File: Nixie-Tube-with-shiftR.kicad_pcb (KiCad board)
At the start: 2 copper layers, 35.5 x 44 mm, 55 parts, among them J1 Conn_01x05_Male, J2 Conn_01x01_Female, J3 Conn_01x05_Female, J4 Conn_01x01_Male, Q1 MMBTA42LT1, Q10 MMBTA42LT1, Q11 AO3400, Q12 AO3400, Q13 AO3400, Q14 MMBTA42LT1, Q15 MMBTA42LT1, Q2 MMBTA42LT1, Q3 MMBTA42LT1, Q4 MMBTA42LT1, Q5 MMBTA42LT1, Q6 MMBTA42LT1, Q7 MMBTA42LT1, Q8 MMBTA42LT1, Q9 MMBTA42LT1, U1 74HC595D, U2 nixie-tube, U3 74HC595D, U4 ams1117-5.0

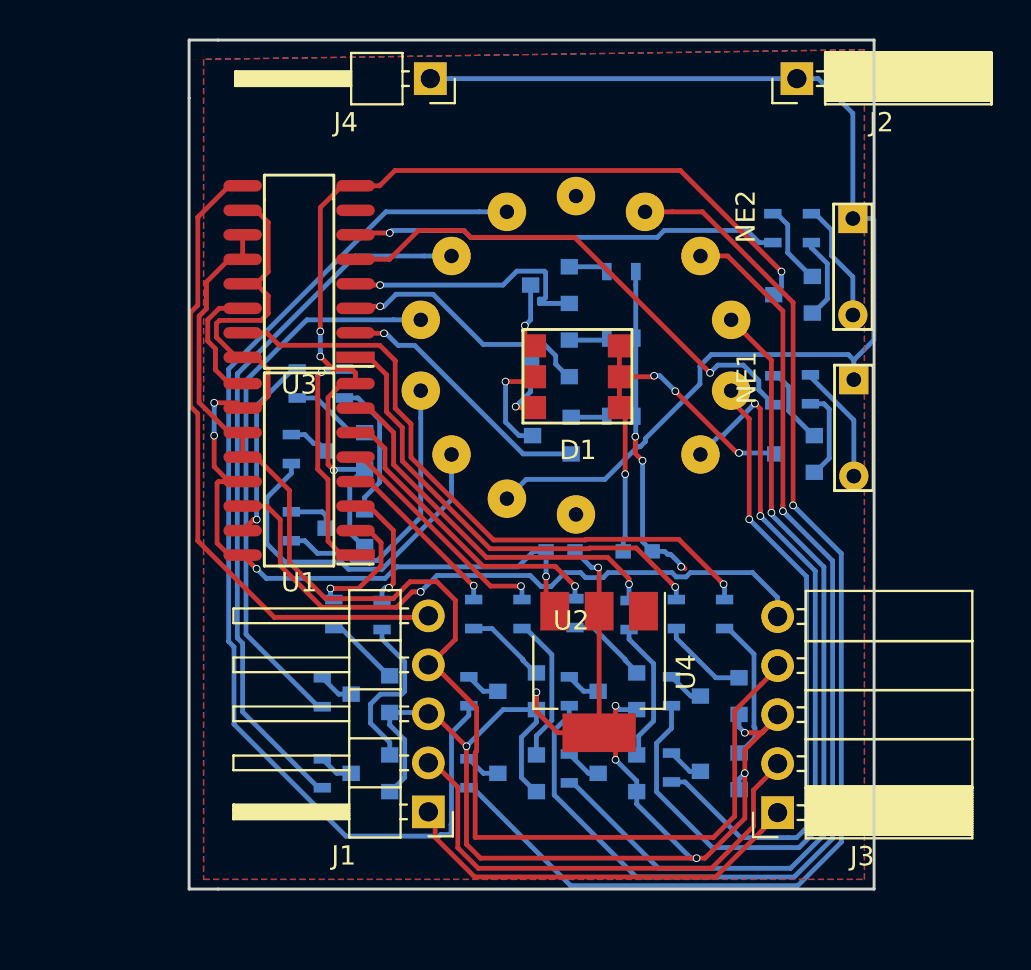
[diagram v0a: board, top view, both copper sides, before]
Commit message: modify board layout dimension text
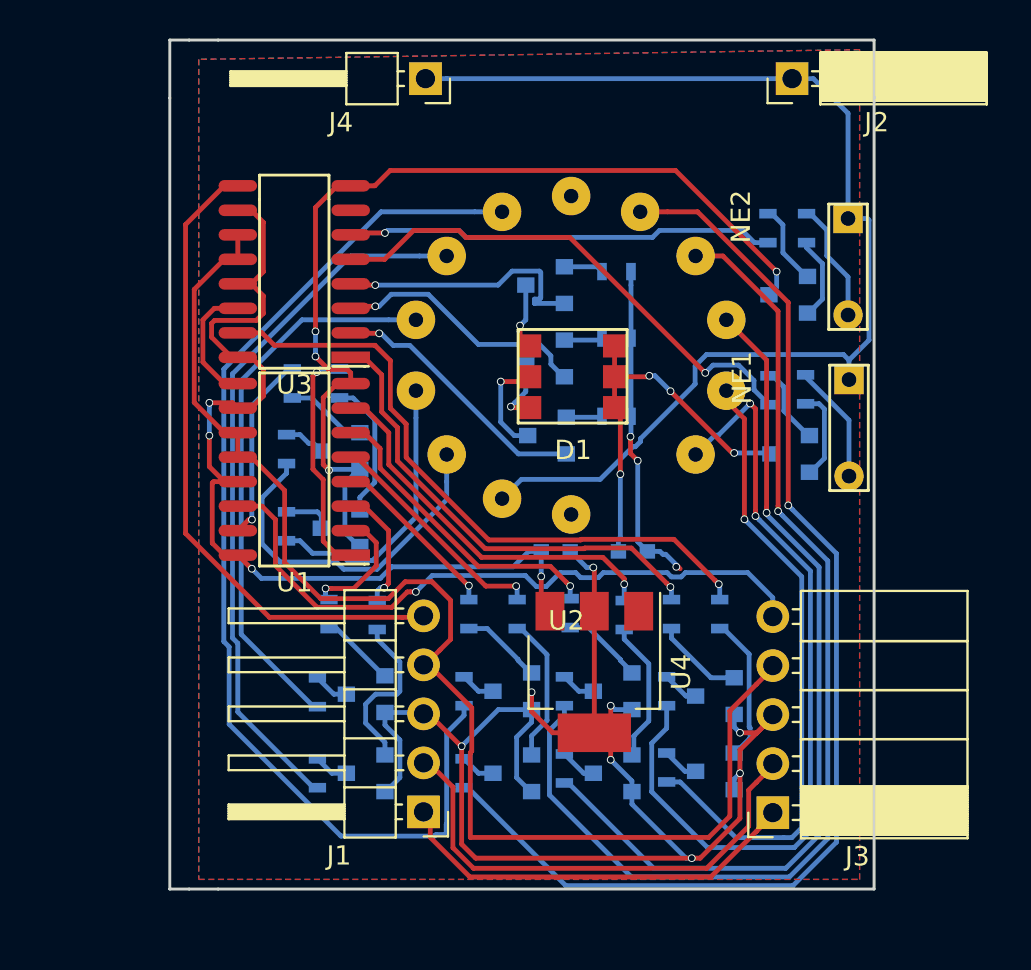
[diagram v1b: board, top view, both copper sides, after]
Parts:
- moved C1 0.25 mm to (175.5, 70.5)
- moved C2 0.25 mm to (171.5, 70.5)
- moved D1 0.25 mm to (172.4, 61.4)
- moved J1 0.25 mm to (164.7, 84.0)
- moved J2 0.25 mm to (183.8, 46.0)
- moved J3 0.25 mm to (182.8, 84.0)
- moved J4 0.25 mm to (164.8, 46.0)
- moved NE1 0.25 mm to (186.7, 61.6)
- moved NE2 0.25 mm to (186.7, 53.2)
- moved Q1 0.25 mm to (160.3, 65.3)
- moved Q10 0.25 mm to (169.2, 77.8)
- moved Q11 0.25 mm to (171.1, 64.5)
- moved Q12 0.25 mm to (170.9, 60.5)
- moved Q13 0.25 mm to (170.9, 56.7)
- moved Q14 0.25 mm to (183.7, 65.5)
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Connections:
- J1 pad 5: /MOSI -> /MOSI-OUT
- J3 pad 5: /MOSI-OUT -> /MOSI
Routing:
- net /MOSI: track 45.5 -> 34.6 mm
- net /MOSI-OUT: track 22.7 -> 33.7 mm
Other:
- board size 35.5 x 44 mm -> 36.5 x 44 mm
- board text added: "36.5x44mm"
- board text removed: "34x44mm"

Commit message: fix track being too near to border line
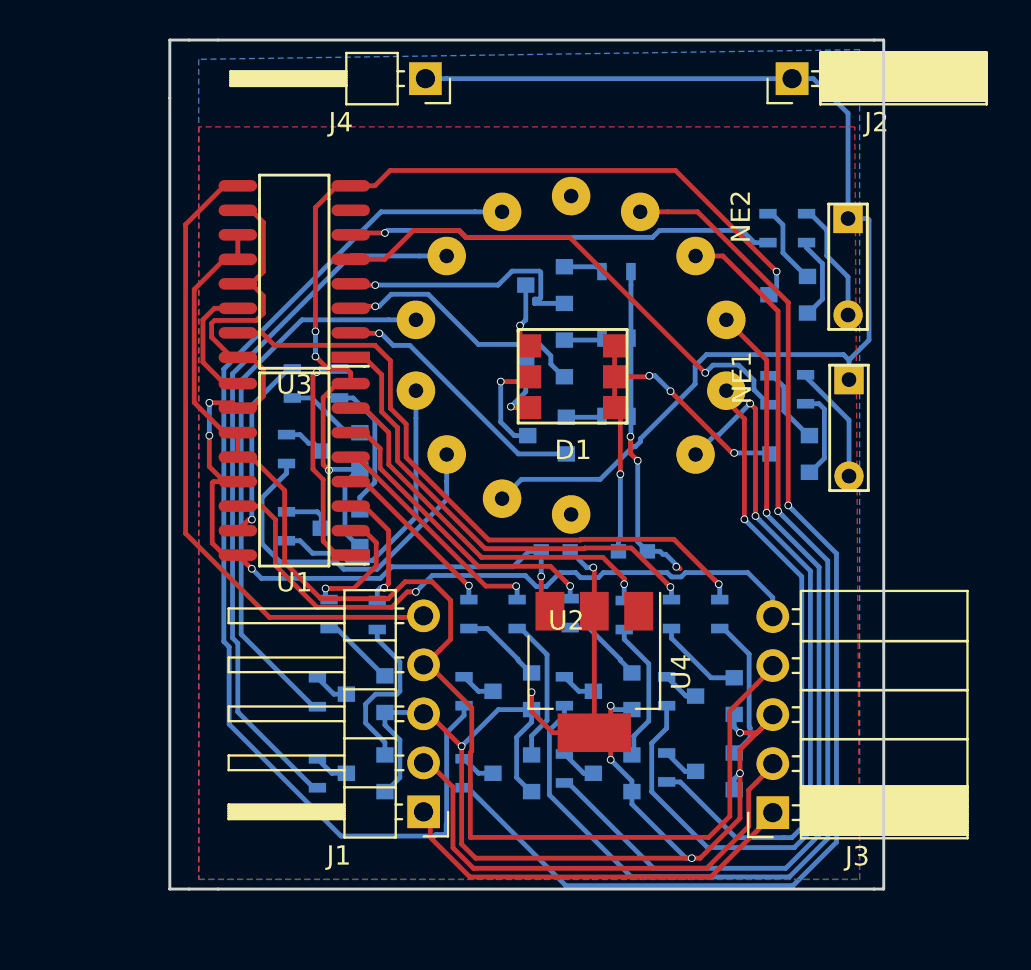
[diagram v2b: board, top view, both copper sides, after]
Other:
- board size 36.5 x 44 mm -> 37 x 44 mm
- board text added: "37x44mm"
- board text removed: "36.5x44mm"
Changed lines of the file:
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@@
     (links 105)
     (no_connects 0)
-    (area 151.424999 43.924999 188.075001 88.075001)
+    (area 151.424999 42.755 195.925239 91.35)
     (thickness 1.6)
-    (drawings 11)
+    (drawings 13)
     (tracks 662)
     (zones 0)
@@
     )
   )
+  (gr_line (start 188.5 88) (end 188 88) (layer Edge.Cuts) (width 0.15))
+  (gr_line (start 188 44) (end 188.5 44) (layer Edge.Cuts) (width 0.15))
   (gr_line (start 152.5 88) (end 151.5 88) (layer Edge.Cuts) (width 0.15))
   (gr_line (start 152.5 44) (end 151.5 44) (layer Edge.Cuts) (width 0.15))
   (gr_line (start 154 88) (end 152.5 88) (layer Edge.Cuts) (width 0.15))
   (gr_line (start 154 44) (end 152.5 44) (layer Edge.Cuts) (width 0.15))
-  (gr_text 36.5x44mm (at 170.25 90) (layer Eco1.User)
+  (gr_text 37x44mm (at 170.25 90) (layer Eco1.User)
     (effects (font (size 1.5 1.5) (thickness 0.3)))
   )
-  (gr_line (start 188 44) (end 188 47) (layer Edge.Cuts) (width 0.15))
+  (gr_line (start 188.5 44) (end 188.5 47) (layer Edge.Cuts) (width 0.15))
   (gr_line (start 154 44) (end 188 44) (layer Edge.Cuts) (width 0.15))
   (gr_line (start 151.5 47) (end 151.5 44) (layer Edge.Cuts) (width 0.15))
-  (gr_line (start 188 88) (end 188 47) (layer Edge.Cuts) (width 0.15))
+  (gr_line (start 188.5 88) (end 188.5 47) (layer Edge.Cuts) (width 0.15))
   (gr_line (start 154 88) (end 188 88) (layer Edge.Cuts) (width 0.15))
   (gr_line (start 151.5 47) (end 151.5 88) (layer Edge.Cuts) (width 0.15))
@@
     (polygon
       (pts
-        (xy 153 45) (xy 153 87.5) (xy 187.25 87.5) (xy 187.25 44.5)
+        (xy 153 48.5) (xy 153 87.5) (xy 187.25 87.5) (xy 187 48.5)
       )
     )

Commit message: modify 9V gnd tracks bigger
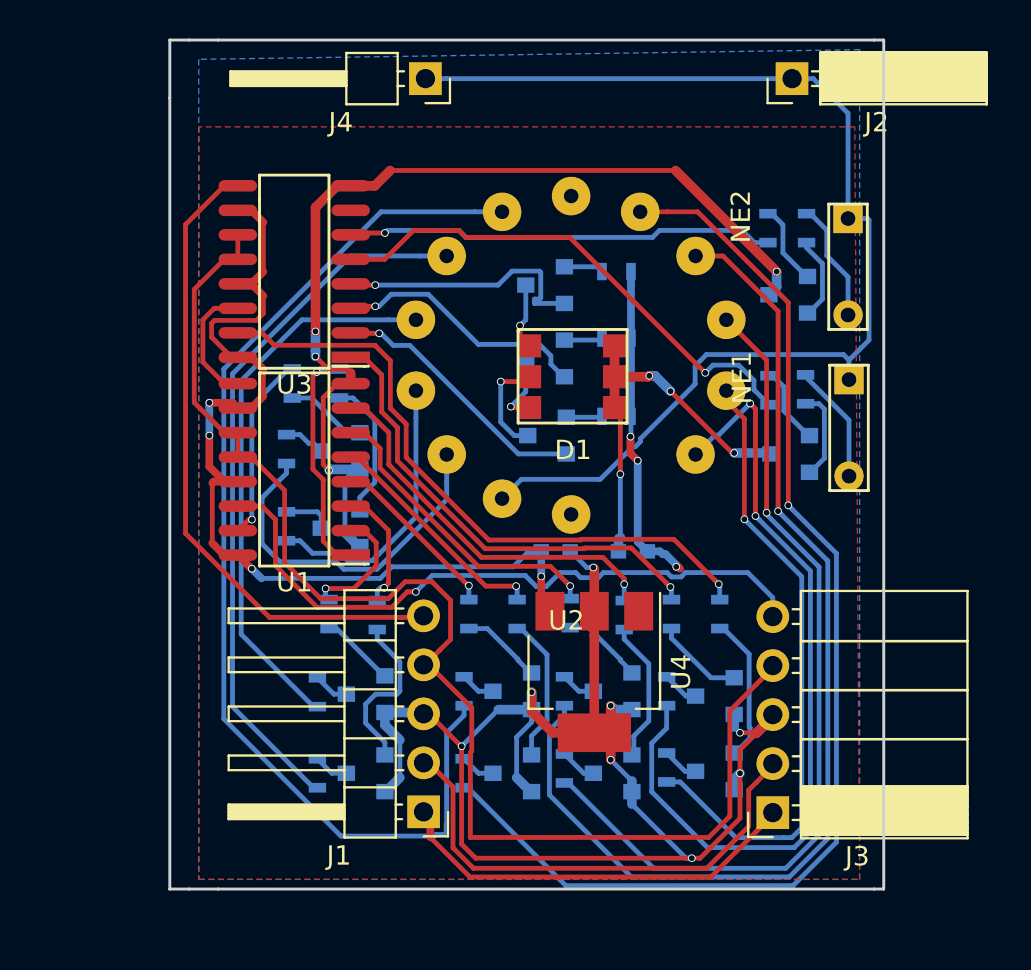
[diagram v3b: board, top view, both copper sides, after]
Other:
- net class GND added: clearance 0.2, trace_width 0.5, via_dia 0.4, via_drill 0.3

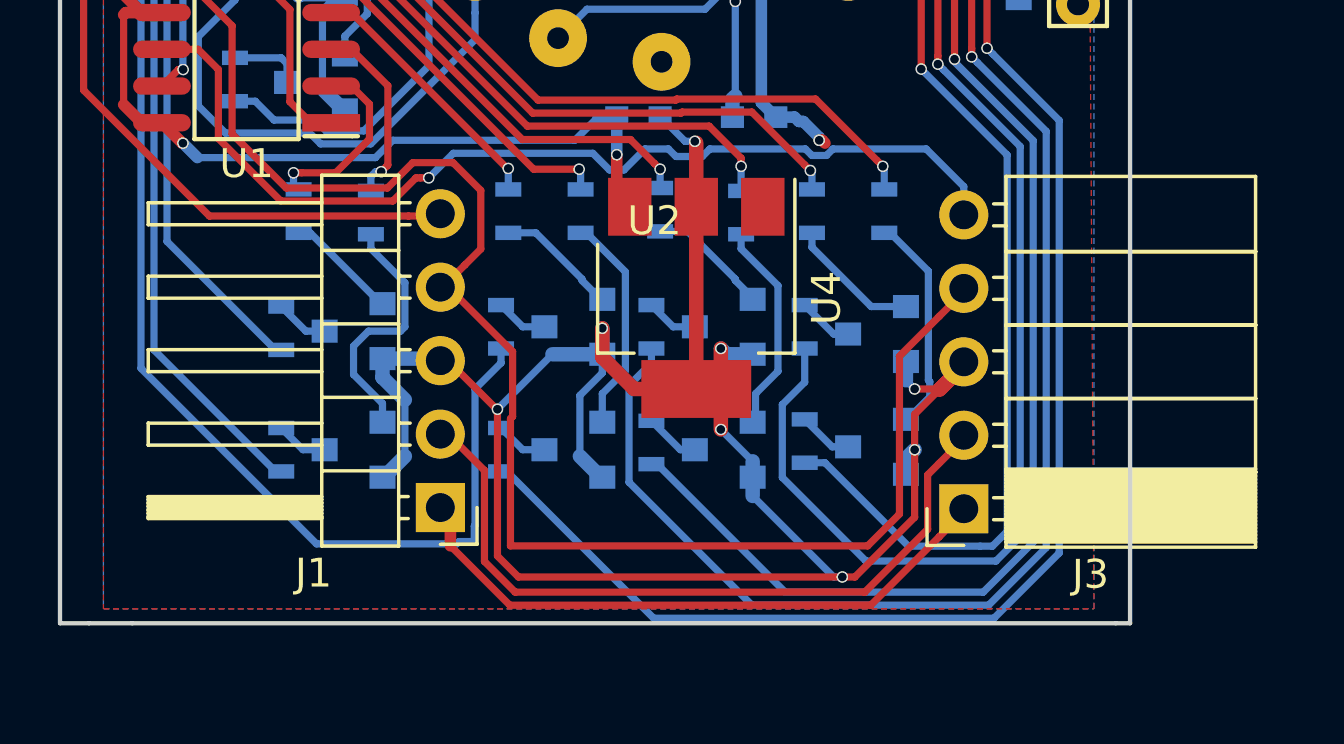
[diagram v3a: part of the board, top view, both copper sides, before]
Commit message: added OE to the pins
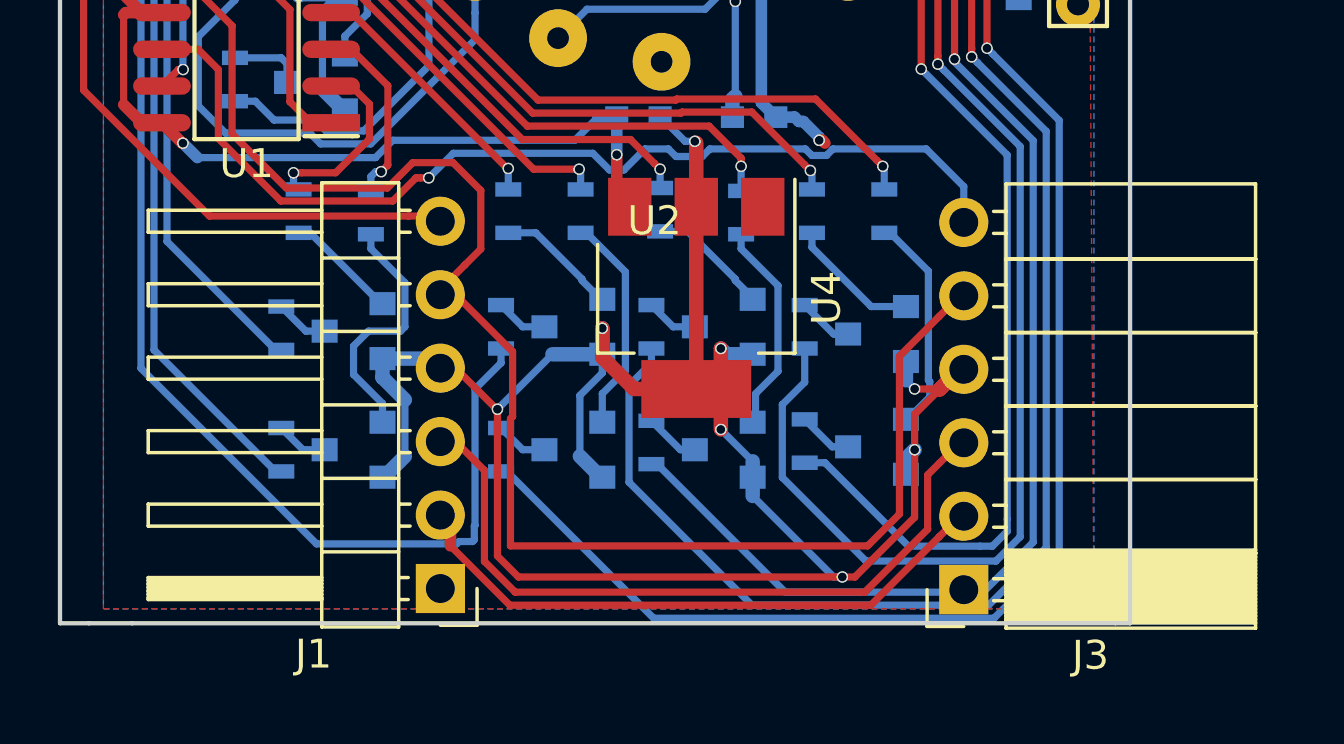
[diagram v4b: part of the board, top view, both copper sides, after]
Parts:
- J1: value Conn_01x05_Male -> Conn_01x06_Male; footprint Pin_Headers:Pin_Header_Angled_1x05_Pitch2.54mm -> Pin_Headers:Pin_Header_Angled_1x06_Pitch2.54mm
- J3: value Conn_01x05_Female -> Conn_01x06_Female; footprint Socket_Strips:Socket_Strip_Angled_1x05_Pitch2.54mm -> Socket_Strips:Socket_Strip_Angled_1x06_Pitch2.54mm
- moved J1 2.80 mm to (164.7, 86.8)
- moved J3 2.80 mm to (182.8, 86.8)
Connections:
- J1 pad 1: +9V -> Net-(J1-Pad1)
- J1 pad 2: /PWREN -> +9V
- J1 pad 3: GND -> /PWREN
- J1 pad 4: /SCK -> GND
- J1 pad 5: /MOSI-OUT -> /SCK
- J3 pad 1: +9V -> Net-(J1-Pad1)
- J3 pad 2: /PWREN -> +9V
- J3 pad 3: GND -> /PWREN
- J3 pad 4: /SCK -> GND
- J3 pad 5: /MOSI -> /SCK
- U1 pad 13: +5V -> Net-(J1-Pad1)
- U3 pad 13: +5V -> Net-(J1-Pad1)
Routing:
- net Net-(J1-Pad1): track 0.00 -> 26.8 mm
- net GND: track 147.8 -> 172.7 mm, vias 16 -> 15
- net /MOSI: track 34.6 -> 12.8 mm, vias 1 -> 0
- net /SCK: track 67.5 -> 47.0 mm
- net /PWREN: track 25.1 -> 8.60 mm, vias 0 -> 1
- net /MOSI-OUT: track 33.7 -> 42.4 mm, vias 0 -> 1
- net +5V: track 50.3 -> 44.7 mm
- net +9V: track 38.2 -> 42.1 mm

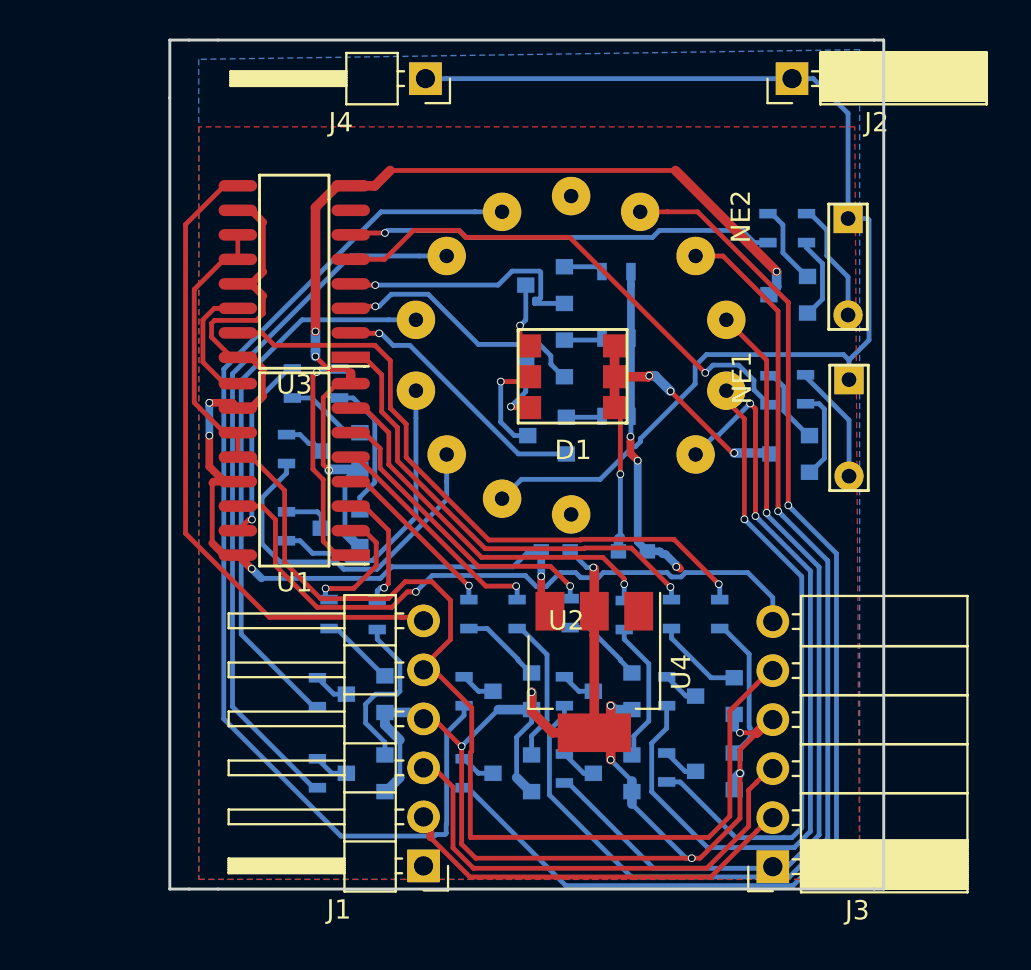
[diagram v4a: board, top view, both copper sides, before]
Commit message: fixed issues on the connectivity on layout
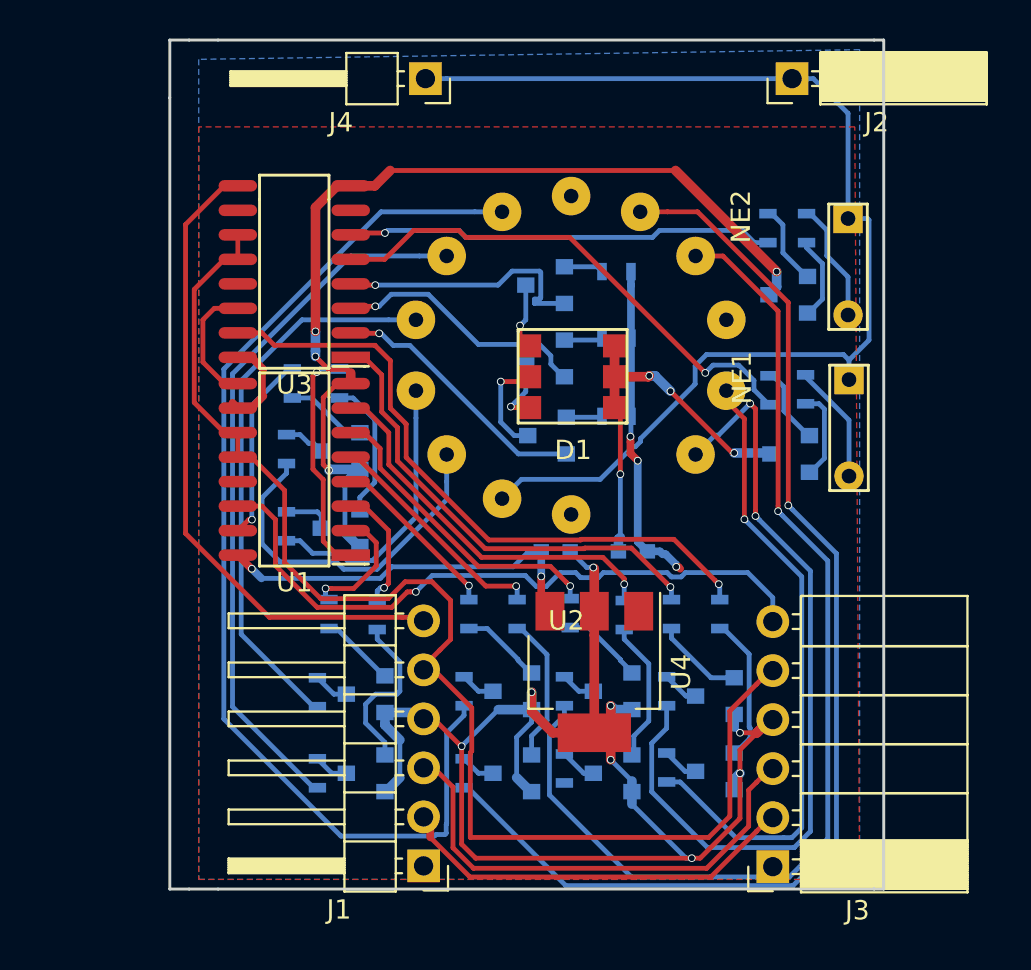
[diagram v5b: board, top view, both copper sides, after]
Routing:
- net Net-(R8-Pad1): track 44.4 -> 0.20 mm, vias 1 -> 0
- net Net-(J1-Pad1): track 26.8 -> 1.40 mm
- net GND: track 172.7 -> 147.8 mm, vias 15 -> 16
- net /MOSI: track 12.8 -> 34.6 mm, vias 0 -> 1
- net /SCK: track 47.0 -> 67.5 mm
- net +5V: track 44.7 -> 26.7 mm, vias 4 -> 2
- net /PWREN: track 8.60 -> 25.1 mm, vias 1 -> 0
- net /MOSI-OUT: track 42.4 -> 33.7 mm, vias 1 -> 0
- net +9V: track 42.1 -> 38.2 mm
